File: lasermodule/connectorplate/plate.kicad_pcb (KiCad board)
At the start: 2 copper layers, 12 x 16.9 mm, 2 parts, among them J1 292173-5, J2 Conn_01x05

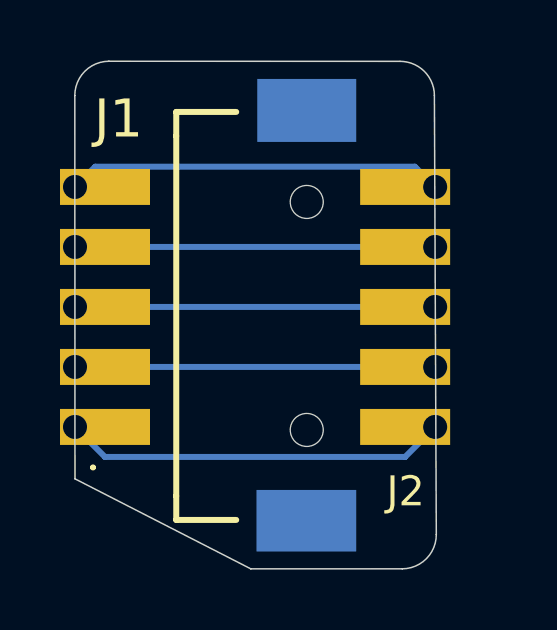
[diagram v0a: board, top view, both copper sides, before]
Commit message: Outside of the format migration, there are only minor component/footprint updates:
base.kicad_sch
J2: Marked as Do Not Populate ((dnp yes)).
J2 footprint: Switched from custom library to standard KiCad library: sockets_scanhead:motor_13pin → Connector_PinSocket_2.00mm:PinSocket_1x13_P2.00mm_Vertical

plate.kicad_sch
Connector footprint: Switched to standard library: mirrormotor:PinHeader_1x05_P2.00mm_Vertical → Connector_PinHeader_2.00mm:PinHeader_1x05_P2.00mm_Vertical
Part order numbers added: Added #manf: M22-2510505, #mouser: 855-M22-2510505, and #farnell: 3226026.
No-connect: Added a (no_connect) symbol on pin coordinate (109.22, 81.28).

mirrormotor.kicad_sch
0 circuit changes: Exactly 4 lines changed outside lib_symbols (the version header). All ~1,486 other lines are symbol cache syntax additions.
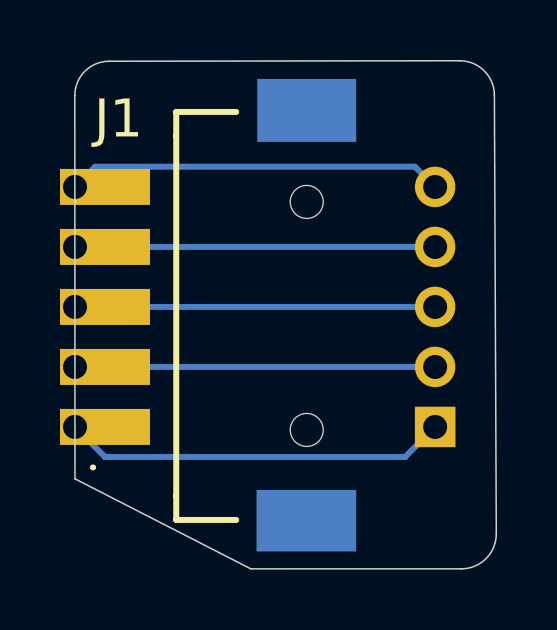
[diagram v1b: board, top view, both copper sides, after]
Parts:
- J2: footprint mirrormotor:PinHeader_1x05_P2.00mm_Vertical -> Connector_PinHeader_2.00mm:PinHeader_1x05_P2.00mm_Vertical; moved to B.Cu
- turned J2 to 0 degrees
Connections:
- J1 pad MP: (no net) -> unconnected-(J1-MountPin-PadMP)
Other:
- board size 12 x 16.9 mm -> 14 x 16.9 mm

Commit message: simplified connector plate, m3 screws maxwell holder
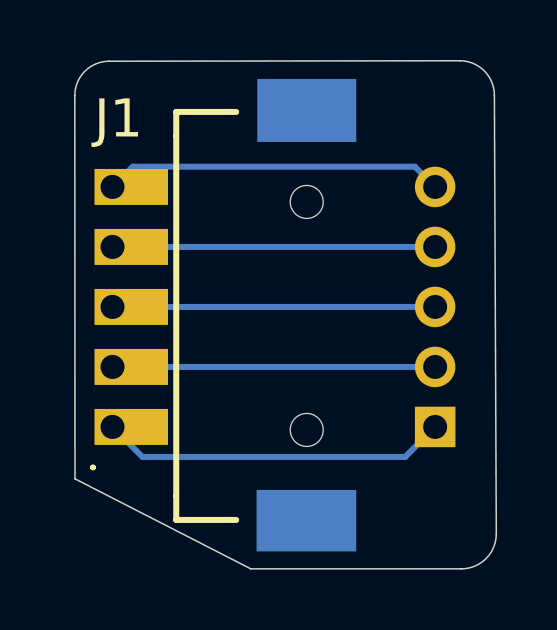
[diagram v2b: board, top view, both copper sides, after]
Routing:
- net Net-(J1-Pin_5): track 12.6 -> 11.3 mm
- net Net-(J1-Pin_4): track 12.0 -> 10.8 mm
- net Net-(J1-Pin_3): track 12.0 -> 10.8 mm
- net Net-(J1-Pin_2): track 12.0 -> 10.8 mm
- net Net-(J1-Pin_1): track 12.8 -> 11.6 mm
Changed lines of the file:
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@@
 		)
 		(pad "1" thru_hole rect
-			(at 3.7 4.5 270)
-			(size 1.2 3)
+			(at 3.7 3.25 270)
+			(size 1.2 2.45)
 			(drill 0.8
-				(offset 0 -1)
+				(offset 0 -0.625)
 			)
-			(property pad_prop_castellated)
-			(layers "*.Cu" "*.Mask")
+			(layers "*.Cu" "*.Paste" "*.Mask")
 			(remove_unused_layers no)
 			(net "Net-(J1-Pin_1)")
@@
 		)
 		(pad "2" thru_hole rect
-			(at 1.7 4.5 270)
-			(size 1.2 3)
+			(at 1.7 3.25 270)
+			(size 1.2 2.45)
 			(drill 0.8
-				(offset 0 -1)
+				(offset 0 -0.625)
 			)
-			(property pad_prop_castellated)
-			(layers "*.Cu" "*.Mask")
+			(layers "*.Cu" "*.Paste" "*.Mask")
 			(remove_unused_layers no)
 			(net "Net-(J1-Pin_2)")
@@
 		)
 		(pad "3" thru_hole rect
-			(at -0.3 4.5 270)
-			(size 1.2 3)
+			(at -0.3 3.25 270)
+			(size 1.2 2.45)
 			(drill 0.8
-				(offset 0 -1)
+				(offset 0 -0.625)
 			)
-			(property pad_prop_castellated)
-			(layers "*.Cu" "*.Mask")
+			(layers "*.Cu" "*.Paste" "*.Mask")
 			(remove_unused_layers no)
 			(net "Net-(J1-Pin_3)")
@@
 		)
 		(pad "4" thru_hole rect
-			(at -2.3 4.5 270)
-			(size 1.2 3)
+			(at -2.3 3.25 270)
+			(size 1.2 2.45)
 			(drill 0.8
-				(offset 0 -1)
+				(offset 0 -0.625)
 			)
-			(property pad_prop_castellated)
-			(layers "*.Cu" "*.Mask")
+			(layers "*.Cu" "*.Paste" "*.Mask")
 			(remove_unused_layers no)
 			(net "Net-(J1-Pin_4)")
@@
 		)
 		(pad "5" thru_hole rect
-			(at -4.3 4.5 270)
-			(size 1.2 3)
+			(at -4.3 3.25 270)
+			(size 1.2 2.45)
 			(drill 0.8
-				(offset 0 -1)
+				(offset 0 -0.625)
 			)
-			(property pad_prop_castellated)
-			(layers "*.Cu" "*.Mask")
+			(layers "*.Cu" "*.Paste" "*.Mask")
 			(remove_unused_layers no)
 			(net "Net-(J1-Pin_5)")
@@
 	(segment
 		(start 148.885 104.61)
-		(end 138.88 104.61)
+		(end 140.13 104.61)
 		(width 0.2)
 		(layer "B.Cu")
@@
 	)
 	(segment
-		(start 138.88 104.61)
-		(end 137.88 103.61)
+		(start 140.13 104.61)
+		(end 139.13 103.61)
 		(width 0.2)
 		(layer "B.Cu")
@@
 	(segment
 		(start 149.885 101.61)
-		(end 137.88 101.61)
+		(end 139.13 101.61)
 		(width 0.2)
 		(layer "B.Cu")
@@
 	(segment
 		(start 149.885 99.61)
-		(end 137.88 99.61)
+		(end 139.13 99.61)
 		(width 0.2)
 		(layer "B.Cu")
@@
 	(segment
 		(start 149.885 97.61)
-		(end 137.88 97.61)
+		(end 139.13 97.61)
 		(width 0.2)
 		(layer "B.Cu")
@@
 	(segment
 		(start 149.21 94.935)
-		(end 138.555 94.935)
+		(end 139.805 94.935)
 		(width 0.2)
 		(layer "B.Cu")
@@
 	)
 	(segment
-		(start 138.555 94.935)
-		(end 137.88 95.61)
+		(start 139.805 94.935)
+		(end 139.13 95.61)
 		(width 0.2)
 		(layer "B.Cu")
